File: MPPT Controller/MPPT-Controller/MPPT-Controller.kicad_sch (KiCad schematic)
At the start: 38 parts, among them J1 Conn_01x02_Pin, J2 Conn_01x02_Pin, J3 Conn_01x02_Pin, J4 USB_C_Receptacle_PowerOnly_6P, K1 JQC-3FF-005-1Z, Q1 BC817, U1 ADS1115IDGS, U2 ESP32-WROOM-32D

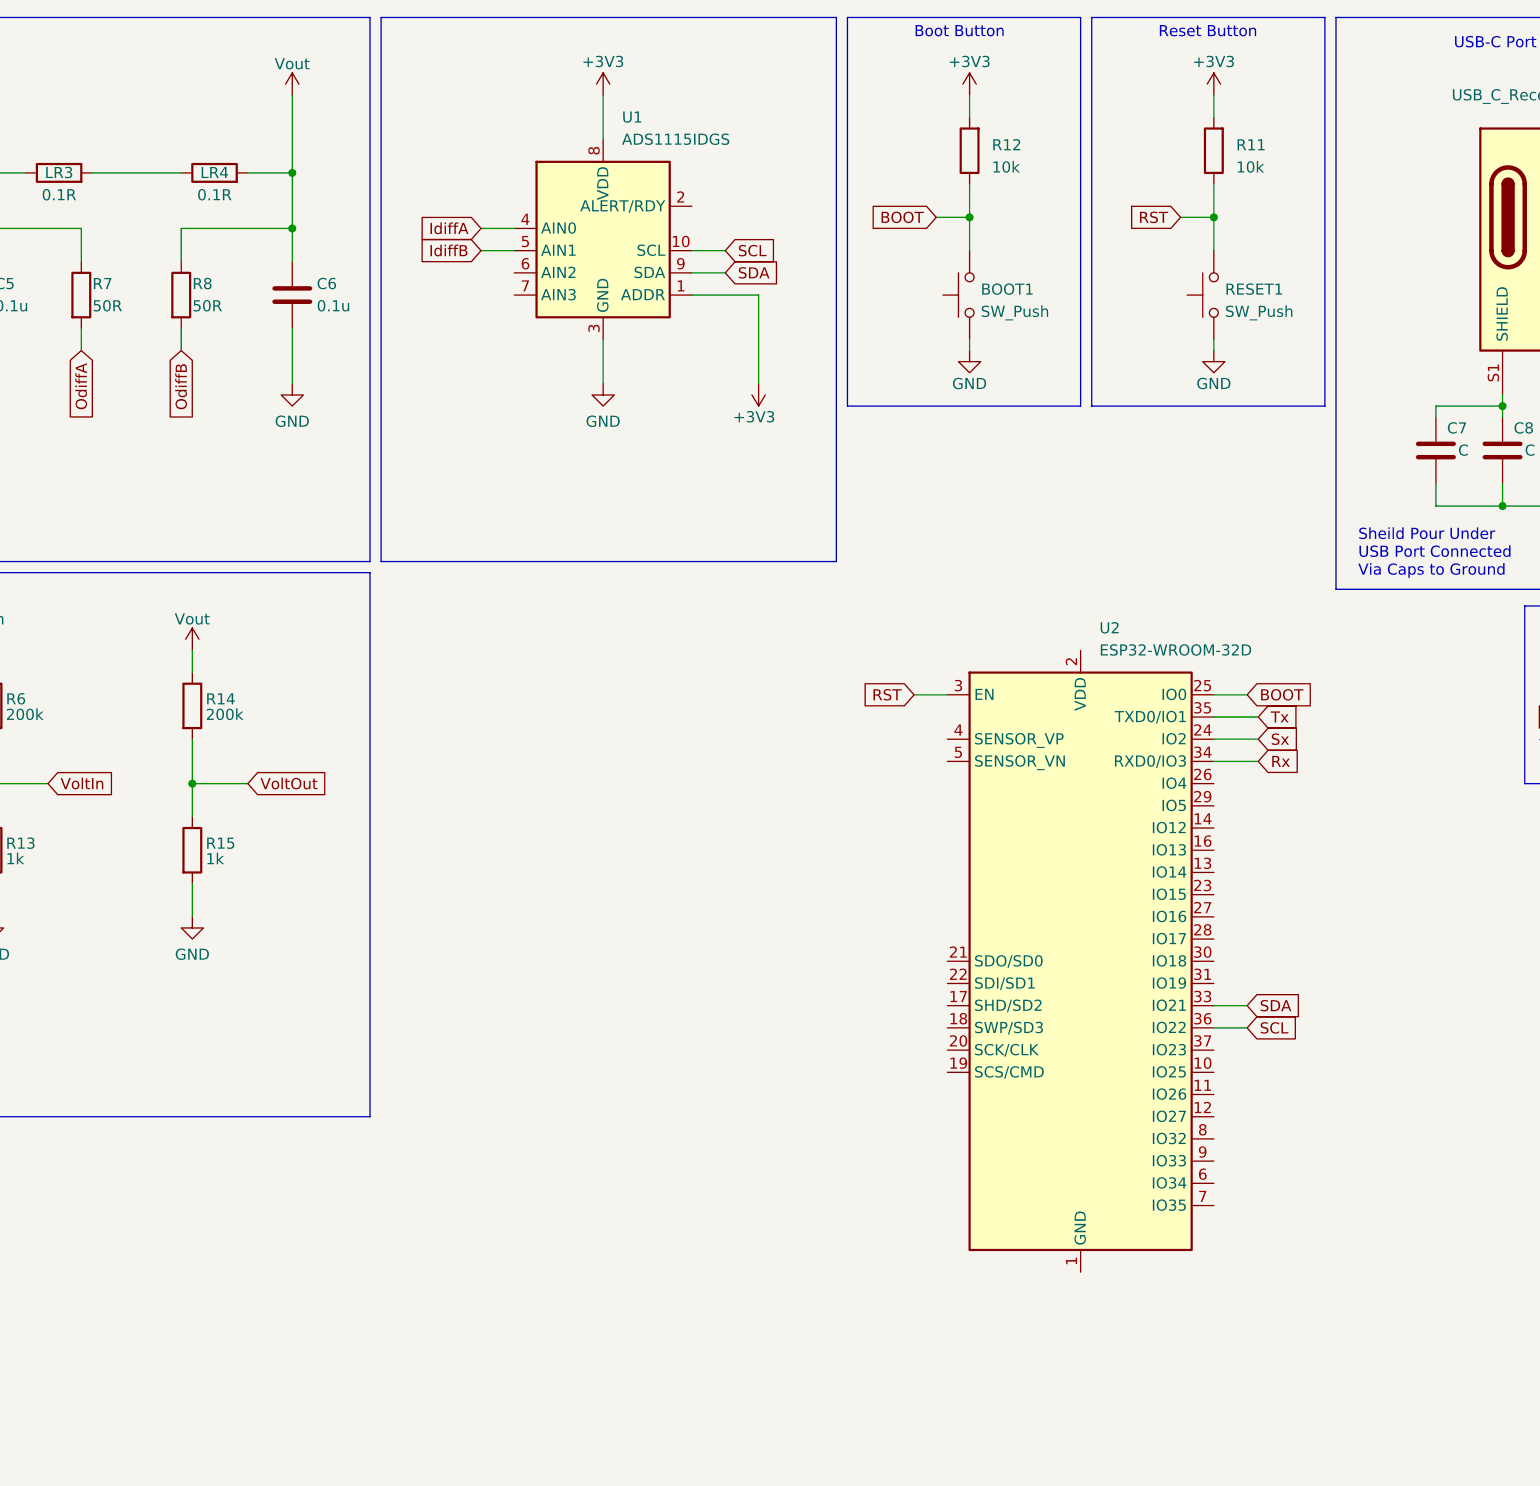
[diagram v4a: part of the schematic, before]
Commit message: Add LED Placeholders
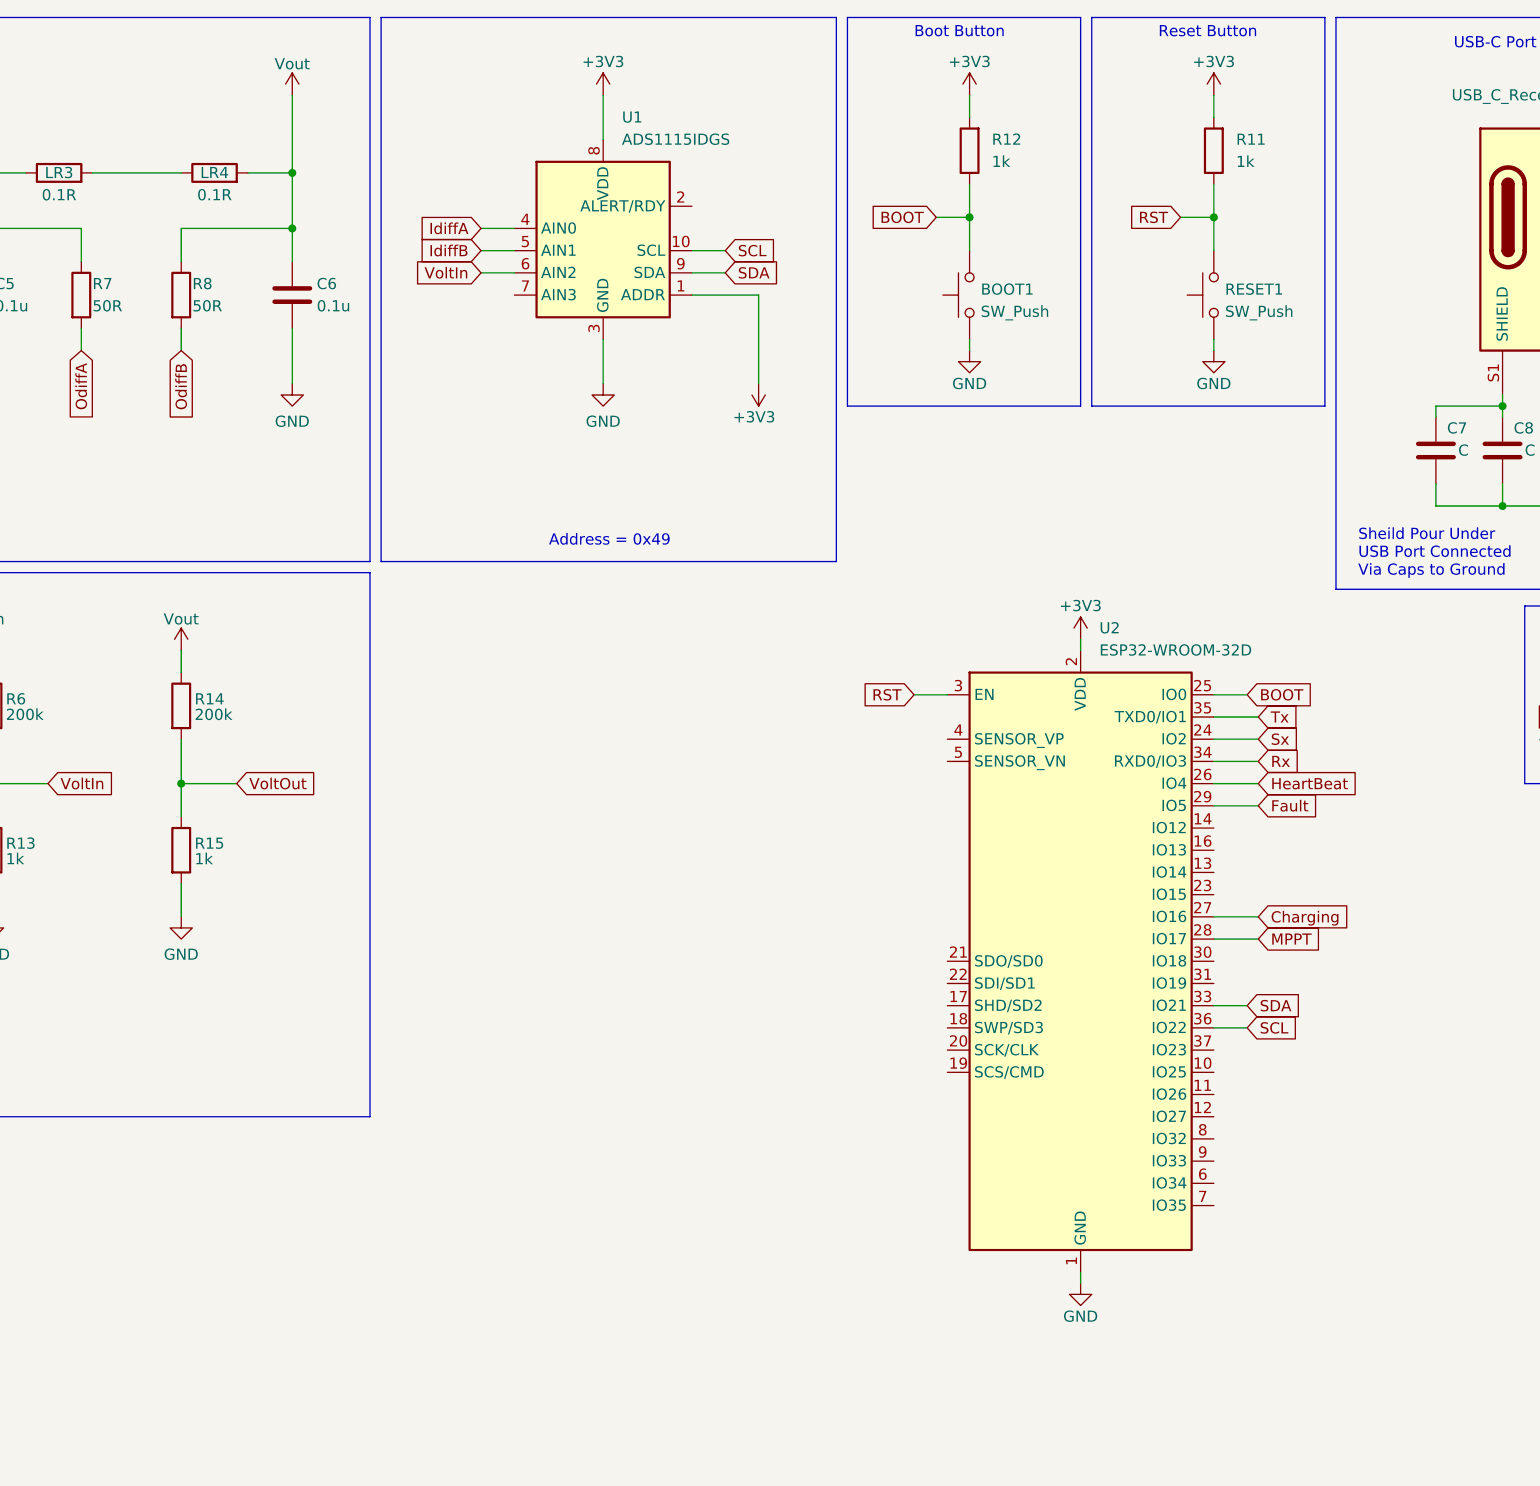
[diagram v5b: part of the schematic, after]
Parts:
- R11, R12: value 10k -> 1k
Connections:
- net +3V3: now also U2.2 (VDD)
- net GND: now also U2.1 (GND), U2.15 (GND), U2.38 (GND), U2.39 (GND)
- net VoltIn: now also U1.6 (AIN2)
- net HeartBeat: now reaches U2.26 (IO4)
- net Charging: now reaches U2.27 (IO16)
- net MPPT: now reaches U2.28 (IO17)
- net Fault: now reaches U2.29 (IO5)
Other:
- note added: "Address = 0x49"
- moved on the sheet: R14, R15

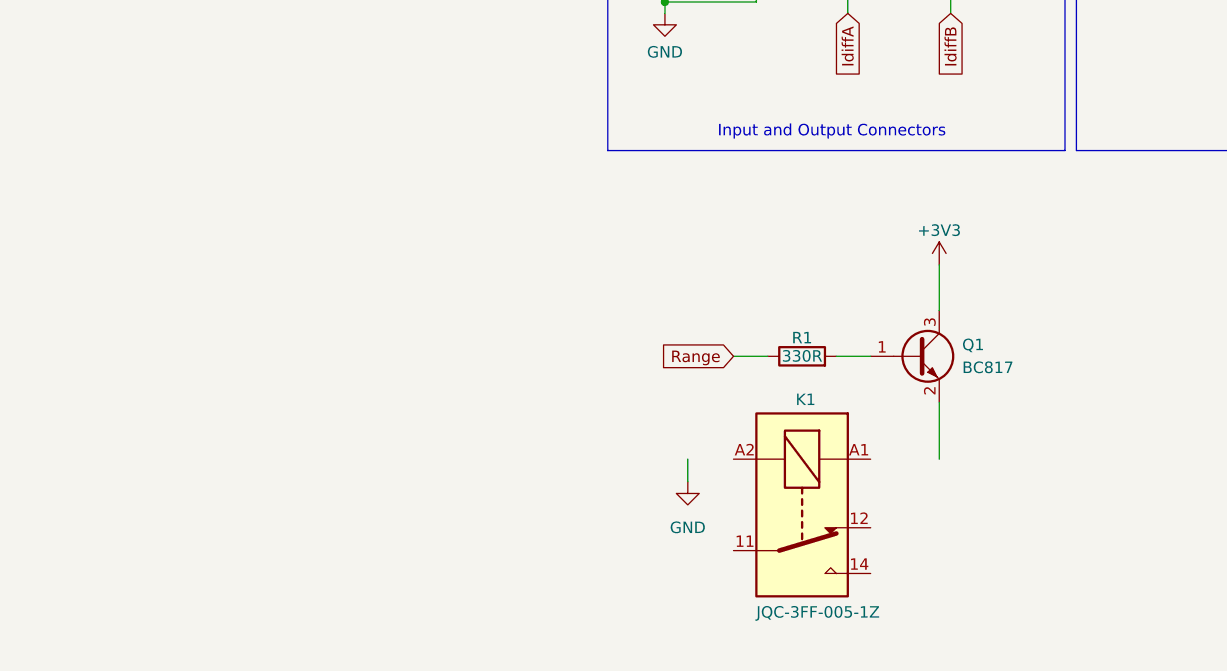
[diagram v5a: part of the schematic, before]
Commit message: Add LEDs
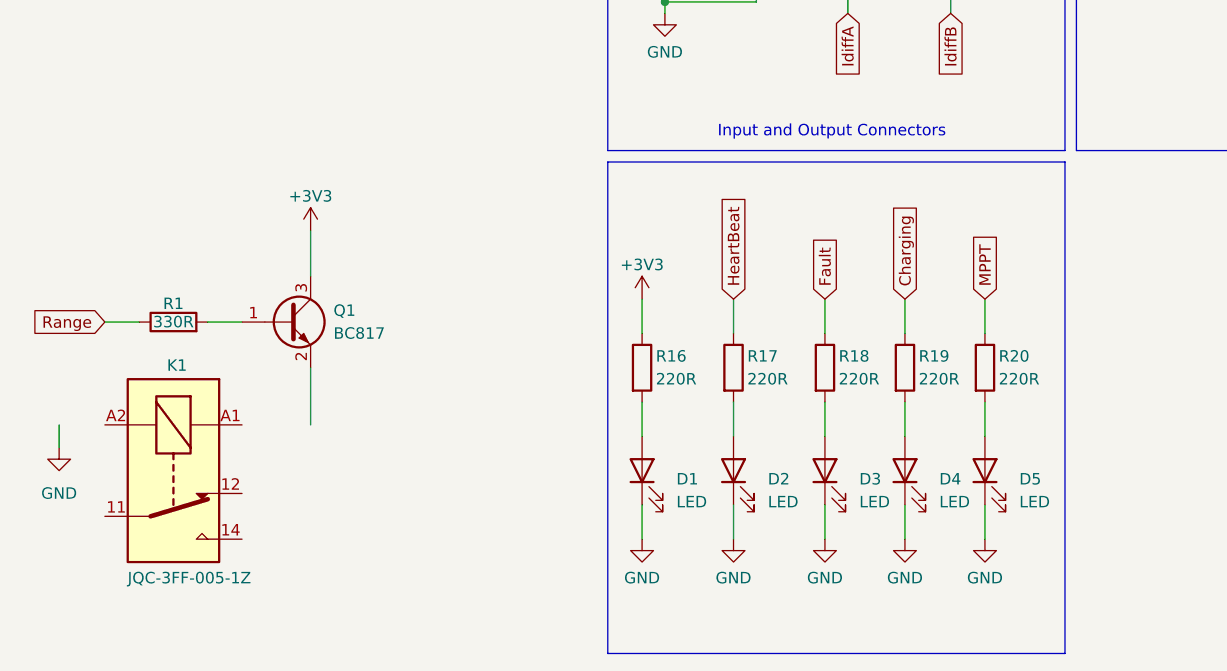
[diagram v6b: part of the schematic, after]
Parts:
- added D1, D2, D3, D4, D5: LED, LED_SMD:LED_1206_3216Metric_Pad1.42x1.75mm_HandSolder, symbol Device:LED
- added R16, R17, R18, R19, R20: 220R, LED_SMD:LED_0805_2012Metric_Pad1.15x1.40mm_HandSolder, symbol Device:R
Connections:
- net +3V3: now also R16.1
- net Charging: now also R19.1
- net Fault: now also R18.1
- net GND: now also D1.1 (K), D2.1 (K), D3.1 (K), D4.1 (K), D5.1 (K)
- net HeartBeat: now also R17.1
- net MPPT: now also R20.1
- new net: D5.2 (A), R20.2
- new net: D1.2 (A), R16.2
- new net: D4.2 (A), R19.2
- new net: D3.2 (A), R18.2
- new net: D2.2 (A), R17.2
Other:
- moved on the sheet: K1, Q1, R1

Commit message: add
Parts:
- added SW1: SW_SPDT, symbol Switch:SW_SPDT
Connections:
- net Vaux: now also SW1.1 (A)
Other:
- moved on the sheet: R13, R14, R15, R6, U2

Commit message: Data Pins
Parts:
- removed J4: USB_C_Receptacle_PowerOnly_6P, CustomLibrary:USB-C Receptacle Power Only THT, symbol Connector:USB_C_Receptacle_PowerOnly_6P
- added J5: USB_C_Receptacle_USB2.0_16P, Connector_USB:USB_C_Receptacle_GCT_USB4085, symbol Connector:USB_C_Receptacle_USB2.0_16P
- added U3: CH340C, Package_SO:SOIC-16_3.9x9.9mm_P1.27mm, symbol Interface_USB:CH340C
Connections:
- net +5V: now also J5.A4 (VBUS), J5.A9 (VBUS), J5.B4 (VBUS), J5.B9 (VBUS)
- net GND: now also J5.A1 (GND), J5.A12 (GND), J5.B1 (GND), J5.B12 (GND)
- net Vaux: no longer SW1.1 (A)
- net at R10.1: now also J5.A5 (CC1)
- net at R9.1: now also J5.B5 (CC2)
- net at C7.1, C8.1: now also J5.S1 (SHIELD)
- new net D+: J5.A6 (D+), J5.B6 (D+)
- new net D-: J5.A7 (D-), J5.B7 (D-)
- no-connect marks 0 -> 2
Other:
- moved on the sheet: C7, C8, FLASH1, R10, R9, SW1
